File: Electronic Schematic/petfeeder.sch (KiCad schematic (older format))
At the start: 7 parts, among them U2 4022, U6 NE555P

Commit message: Hadware 100%
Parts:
- removed C1: 150uF, symbol Device:C
- removed C2: 10pF, symbol Device:C
- removed R6: 2.2kR, symbol Device:R
- removed R7: 200R, symbol Device:R
- removed U2: 4022, symbol 4xxx:4022
- removed U6: NE555P, Package_DIP:DIP-8_W7.62mm, symbol Timer:NE555P
- removed U?: PIC16F84A-XXP, symbol MCU_Microchip_PIC16:PIC16F84A-XXP
- added C3: 10uF, symbol Device:C
- added C4, C5, C7: C, symbol Device:C
- added C6: CP, symbol Device:CP
- added D1, D2: 1N4001, Diode_THT:D_DO-41_SOD81_P10.16mm_Horizontal, symbol Diode:1N4001
- added J1: Ext. UART Conn., symbol Connector:Conn_01x04_Female
- added J2: Ext. Motor Conn., symbol Connector:Conn_01x02_Male
- added J3: Ext. Servo Conn., symbol Connector:Conn_01x03_Female
- added J5: Ext. Keyboard Conn., symbol Connector:Conn_01x08_Male
- added J6: Ext. Balance Conn., symbol Connector:Conn_01x03_Male
- added J7: Ext. AC Input Conn., symbol Connector:Screw_Terminal_01x02
- added J8: Ext. LCD Conn., symbol Connector:Conn_01x14_Female
- added J9: Flash Setup, symbol Connector_Generic:Conn_02x02_Counter_Clockwise
- added Q1: BC237, Package_TO_SOT_THT:TO-92_Inline, symbol Transistor_BJT:BC237
- added R1, R11, R12, R13, R5: 10kR, symbol Device:R
- added R14: 330R, symbol Device:R
- added R2: R, symbol Device:R
- added R3, R4: 1kR, symbol Device:R
- added RV1: R_POT_TRIM, symbol Device:R_POT_TRIM
- added T1: Transformer_1P_SS, symbol Device:Transformer_1P_SS
- added U1: ESP-12F, RF_Module:ESP-12E, symbol RF_Module:ESP-12F
- added U3: DS1307+, Package_DIP:DIP-8_W7.62mm, symbol Timer_RTC:DS1307+
- added U4: IFX27001TFV33, Package_TO_SOT_SMD:TO-252-3_TabPin2, symbol Regulator_Linear:IFX27001TFV33
- added U5: L7805, symbol Regulator_Linear:L7805
- added U9: 24LC01, symbol Memory_EEPROM:24LC01
- added Y1: 32kHz, symbol Device:Crystal
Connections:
- net +5V: now also J2.2 (Pin_2), J3.1 (Pin_1), J6.1 (Pin_1), R14.1, R3.1, R4.1, RV1.3, U3.3 (VBAT), U3.8 (VCC), U4.3 (I), U9.8 (VCC)
- net GND: now also C3.2, C4.2, C5.2, C6.2, C7.2, J1.4 (Pin_4), J3.3 (Pin_3), J6.3 (Pin_3), J8.1 (Pin_1), J8.5 (Pin_5), Q1.3 (E), R13.2, RV1.1, T1.4 (SC), U1.15 (GND), U3.4 (GND), U4.1 (GND), U5.2 (GND), U9.4 (GND), U9.7 (WP)
- net column1: now also J5.1 (Pin_1)
- net column2: now also J5.2 (Pin_2)
- net column3: now also J5.3 (Pin_3)
- net column4: now also J5.4 (Pin_4)
- new net: R1.1, U1.1 (~RST)
- new net: J9.1 (Pin_1), J9.2 (Pin_2), U1.16 (GPIO15)
- new net: R12.1, U1.17 (GPIO2)
- new net: R11.1, U1.3 (EN)
- new net: U3.1 (X1), Y1.2
- new net: U3.2 (X2), Y1.1
- new net: Q1.2 (B), R2.1
- new net: J1.1 (Pin_1), R5.2
- new net: D1.2 (A), T1.5 (SB)
- new net: J7.2 (Pin_2), T1.1 (AA)
- new net: J7.1 (Pin_1), T1.2 (AB)
- new net: D2.2 (A), T1.3 (SA)
- new net: J8.2 (Pin_2), R14.2
- new net: J9.3 (Pin_3), R13.1
- new net +3.3V_OUT: C7.1, U4.2 (Q)
- new net +3V3: C3.1, R1.2, R11.2, R12.2, U1.8 (VCC)
- new net +5V_OUT: C5.1, U5.3 (OUT)
- new net RET_OUT: C4.1, C6.1, D1.1 (K), D2.1 (K), U5.1 (IN)
- new net RX: J1.3 (Pin_3), U1.21 (GPIO3/RXD)
- new net SCL: R4.2, U1.20 (GPIO5), U3.6 (SCL), U9.6 (SCL)
- new net SDA: R3.2, U1.19 (GPIO4), U3.5 (SDA), U9.5 (SDA)
- new net TX: J1.2 (Pin_2), U1.22 (GPIO1/TXD)
- new net balança: J6.2 (Pin_2), U1.2 (ADC)
- new net clk_lcd: U1.6 (GPIO12)
- new net data4: J8.11 (Pin_11)
- new net data5: J8.12 (Pin_12)
- new net data6: J8.13 (Pin_13)
- new net data7: J8.14 (Pin_14)
- new net en: J8.6 (Pin_6)
- new net flash: R5.1, U1.18 (GPIO0)
- new net line1: J5.5 (Pin_5)
- new net line2: J5.6 (Pin_6)
- new net line3: J5.7 (Pin_7)
- new net line4: J5.8 (Pin_8)
- new net motor: R2.2, U1.4 (GPIO16)
- new net motor-: J2.1 (Pin_1), Q1.1 (C)
- new net rs: J8.4 (Pin_4)
- new net rx_lcd: U1.5 (GPIO14)
- new net servo: J3.2 (Pin_2), J9.4 (Pin_4)
- new net trimpot: J8.3 (Pin_3), RV1.2
- new net tx_lcd: U1.7 (GPIO13)
- no-connect marks 6 -> 14
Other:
- note added: "Engines Circuits"
- note added: "External LCD and Keyboard Circuits"
- note added: "Linear Retifier and Regulator Circuit\n"
- note added: "Main Circuit\n\n"
- note removed: "Keyboard's columns pulser\n"

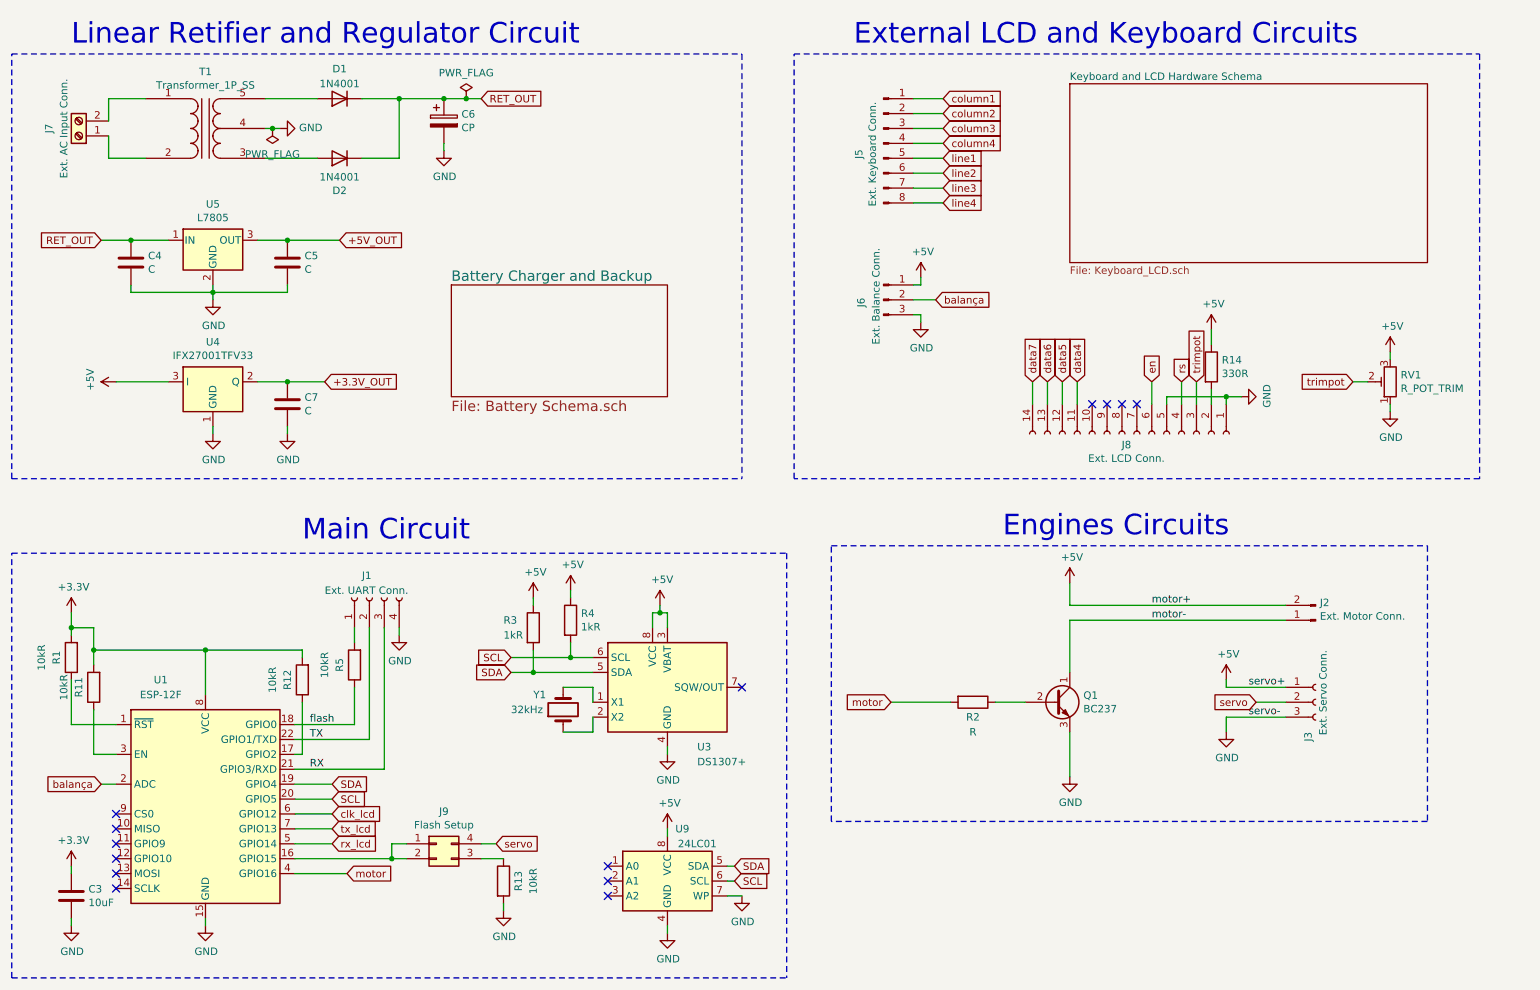
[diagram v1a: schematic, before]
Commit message: Correcoes Esquematico e Avanço codigo esp
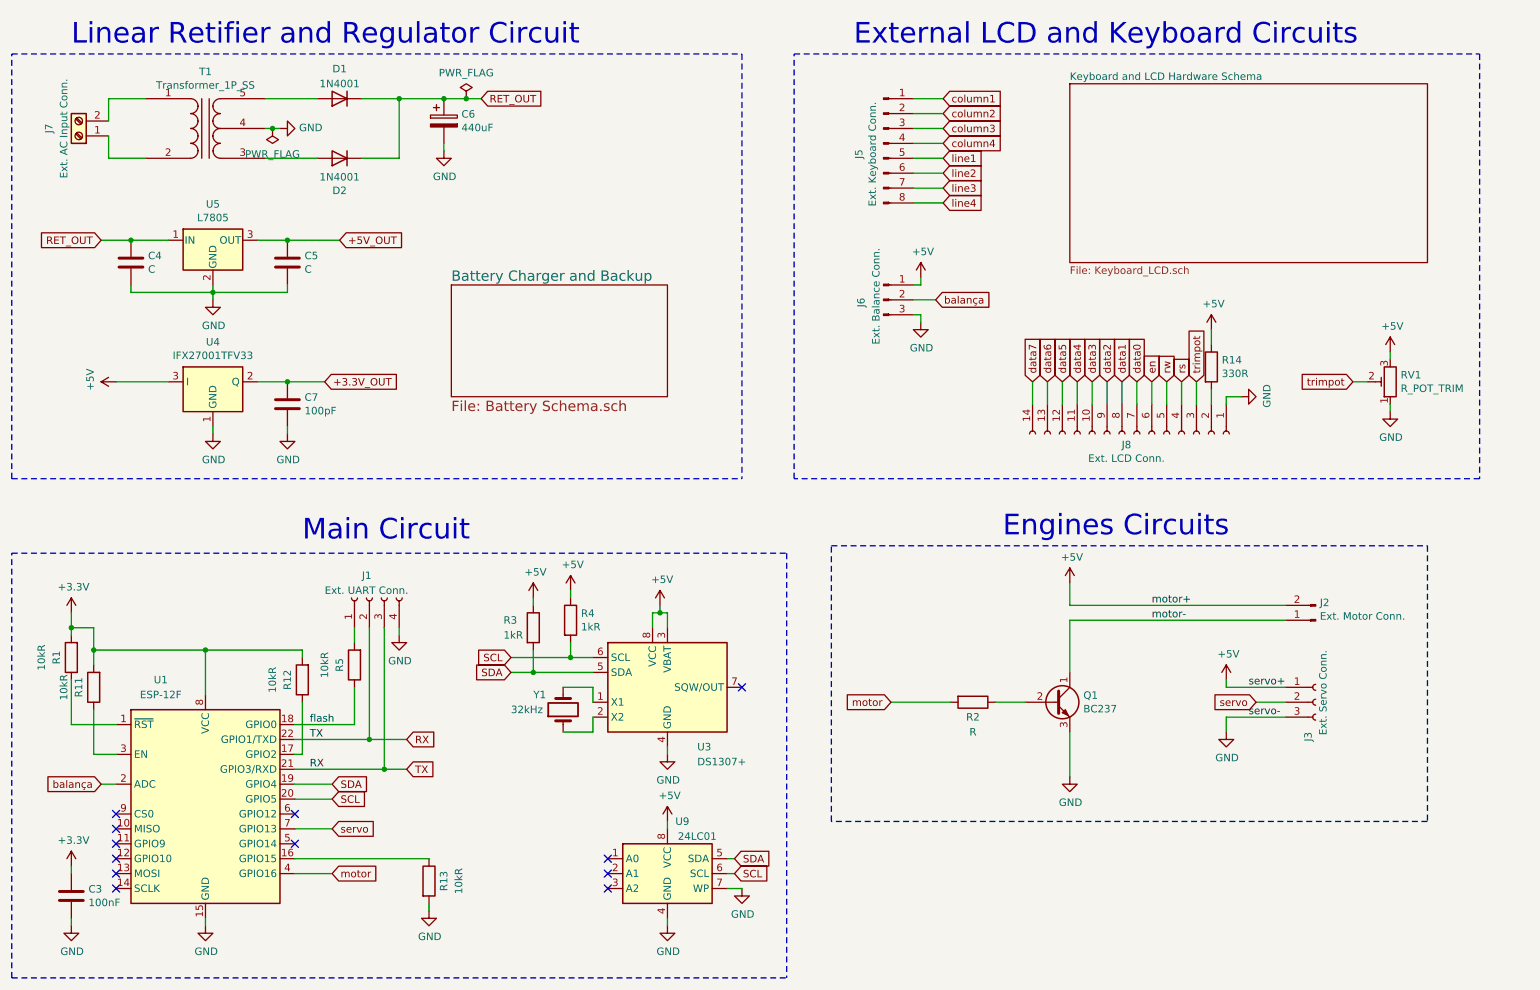
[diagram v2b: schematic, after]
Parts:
- removed J9: Flash Setup, symbol Connector_Generic:Conn_02x02_Counter_Clockwise
- C3: value 10uF -> 100nF
- C6: value CP -> 440uF
- C7: value C -> 100pF
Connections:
- net TX is gone; now on net RX: J1.2 (Pin_2), U1.22 (GPIO1/TXD)
- net tx_lcd is gone; now on net servo: U1.7 (GPIO13)
- net GND: no longer J8.5 (Pin_5)
- net at U1.16 (GPIO15): now also R13.1
- net data3: now reaches J8.10 (Pin_10)
- net data0: now reaches J8.7 (Pin_7)
- net data1: now reaches J8.8 (Pin_8)
- net data2: now reaches J8.9 (Pin_9)
- net clk_lcd: no longer names the net of U1.6 (GPIO12)
- net rx_lcd: no longer names the net of U1.5 (GPIO14)
- new net rw: J8.5 (Pin_5)
- no-connect marks 14 -> 12
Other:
- moved on the sheet: R13, U9
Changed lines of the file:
@@
 Wire Wire Line
 	2300 6900 2300 6850
-Wire Wire Line
-	2900 6550 3250 6550
-Text GLabel 3250 6550 2    50   Input ~ 0
+Text GLabel 3150 6550 2    50   Input ~ 0
 motor
 Text Label 3000 5550 0    50   ~ 0
@@
 Text Notes 6650 1000 0    138  ~ 0
 External LCD and Keyboard Circuits
-Text GLabel 3150 6150 2    50   Input ~ 0
-clk_lcd
-Text GLabel 3150 6250 2    50   Input ~ 0
-tx_lcd
-Text GLabel 3150 6350 2    50   Input ~ 0
-rx_lcd
-Wire Wire Line
-	2900 6350 3150 6350
-Wire Wire Line
-	2900 6250 3150 6250
-Wire Wire Line
-	2900 6150 3150 6150
 Wire Wire Line
 	7050 2050 7250 2050
@@
 P 1400 6700
 F 0 "C3" H 1515 6746 50  0000 L CNN
-F 1 "10uF" H 1515 6655 50  0000 L CNN
+F 1 "100nF" H 1515 6655 50  0000 L CNN
 F 2 "" H 1438 6550 50  0001 C CNN
 F 3 "~" H 1400 6700 50  0001 C CNN
@@
 P 3900 1500
 F 0 "C6" H 4018 1546 50  0000 L CNN
-F 1 "CP" H 4018 1455 50  0000 L CNN
+F 1 "440uF" H 4018 1455 50  0000 L CNN
 F 2 "" H 3938 1350 50  0001 C CNN
 F 3 "~" H 3900 1500 50  0001 C CNN
@@
 P 2850 3400
 F 0 "C7" H 2965 3446 50  0000 L CNN
-F 1 "C" H 2965 3355 50  0000 L CNN
+F 1 "100pF" H 2965 3355 50  0000 L CNN
 F 2 "" H 2888 3250 50  0001 C CNN
 F 3 "~" H 2850 3400 50  0001 C CNN
@@
 EndData
 $EndBitmap
-Text GLabel 4250 6350 2    50   Input ~ 0
+Text GLabel 3150 6250 2    50   Input ~ 0
 servo
 $Comp
-L Connector_Generic:Conn_02x02_Counter_Clockwise J9
-U 1 1 619BBF9D
-P 3850 6350
-F 0 "J9" H 3900 6567 50  0000 C CNN
-F 1 "Flash Setup" H 3900 6476 50  0000 C CNN
-F 2 "" H 3850 6350 50  0001 C CNN
-F 3 "~" H 3850 6350 50  0001 C CNN
-	1    3850 6350
-	1    0    0    -1
-$EndComp
-$Comp
 L Device:R R13
 U 1 1 619DCC8E
-P 4300 6600
-F 0 "R13" V 4400 6600 50  0000 C CNN
-F 1 "10kR" V 4500 6600 50  0000 C CNN
-F 2 "" V 4230 6600 50  0001 C CNN
-F 3 "~" H 4300 6600 50  0001 C CNN
-	1    4300 6600
+P 3800 6600
+F 0 "R13" V 3900 6600 50  0000 C CNN
+F 1 "10kR" V 4000 6600 50  0000 C CNN
+F 2 "" V 3730 6600 50  0001 C CNN
+F 3 "~" H 3800 6600 50  0001 C CNN
+	1    3800 6600
 	1    0    0    -1
 $EndComp
-Wire Wire Line
-	4150 6450 4300 6450
-Wire Wire Line
-	3650 6350 3550 6350
-Wire Wire Line
-	3550 6350 3550 6450
-Connection ~ 3550 6450
-Wire Wire Line
-	3550 6450 3650 6450
 $Comp
 L power:GND #PWR039
 U 1 1 619E8B33
-P 4300 6800
-F 0 "#PWR039" H 4300 6550 50  0001 C CNN
-F 1 "GND" H 4305 6627 50  0000 C CNN
-F 2 "" H 4300 6800 50  0001 C CNN
-F 3 "" H 4300 6800 50  0001 C CNN
-	1    4300 6800
+P 3800 6800
+F 0 "#PWR039" H 3800 6550 50  0001 C CNN
+F 1 "GND" H 3805 6627 50  0000 C CNN
+F 2 "" H 3800 6800 50  0001 C CNN
+F 3 "" H 3800 6800 50  0001 C CNN
+	1    3800 6800
 	1    0    0    -1
 $EndComp
 Wire Wire Line
-	4300 6800 4300 6750
-Wire Wire Line
-	4250 6350 4150 6350
+	3800 6800 3800 6750
 $Comp
 L Device:R R11
@@
 Wire Wire Line
 	8850 3400 8850 3250
-Wire Wire Line
-	9150 3350 8750 3350
-Wire Wire Line
-	8750 3350 8750 3400
-Connection ~ 9150 3350
 Text GLabel 8650 3250 1    50   Input ~ 0
 en
 Wire Wire Line
 	8650 3400 8650 3250
-NoConn ~ 8550 3400
-NoConn ~ 8450 3400
-NoConn ~ 8350 3400
-NoConn ~ 8250 3400
 Text GLabel 8150 3250 1    50   Input ~ 0
 data4
@@
 L Memory_EEPROM:24LC01 U9
 U 1 1 617A6300
-P 5400 6600
-F 0 "U9" H 5500 6950 50  0000 C CNN
-F 1 "24LC01" H 5600 6850 50  0000 C CNN
-F 2 "" H 5400 6600 50  0001 C CNN
-F 3 "http://ww1.microchip.com/downloads/en/DeviceDoc/21711J.pdf" H 5400 6600 50  0001 C CNN
-	1    5400 6600
+P 5400 6550
+F 0 "U9" H 5500 6900 50  0000 C CNN
+F 1 "24LC01" H 5600 6800 50  0000 C CNN
+F 2 "" H 5400 6550 50  0001 C CNN
+F 3 "http://ww1.microchip.com/downloads/en/DeviceDoc/21711J.pdf" H 5400 6550 50  0001 C CNN
+	1    5400 6550
 	1    0    0    -1
 $EndComp
@@
 	4350 5200 4500 5200
 Connection ~ 4500 5200
-Wire Wire Line
-	2900 6450 3550 6450
 $Comp
 L power:GND #PWR048
 U 1 1 617E44D4
-P 5400 6950
-F 0 "#PWR048" H 5400 6700 50  0001 C CNN
-F 1 "GND" H 5405 6777 50  0000 C CNN
-F 2 "" H 5400 6950 50  0001 C CNN
-F 3 "" H 5400 6950 50  0001 C CNN
-	1    5400 6950
+P 5400 6900
+F 0 "#PWR048" H 5400 6650 50  0001 C CNN
+F 1 "GND" H 5405 6727 50  0000 C CNN
+F 2 "" H 5400 6900 50  0001 C CNN
+F 3 "" H 5400 6900 50  0001 C CNN
+	1    5400 6900
 	1    0    0    -1
 $EndComp
@@
 L power:+5V #PWR047
 U 1 1 617EA5A8
-P 5400 6250
-F 0 "#PWR047" H 5400 6100 50  0001 C CNN
-F 1 "+5V" H 5415 6423 50  0000 C CNN
-F 2 "" H 5400 6250 50  0001 C CNN
-F 3 "" H 5400 6250 50  0001 C CNN
-	1    5400 6250
+P 5400 6200
+F 0 "#PWR047" H 5400 6050 50  0001 C CNN
+F 1 "+5V" H 5415 6373 50  0000 C CNN
+F 2 "" H 5400 6200 50  0001 C CNN
+F 3 "" H 5400 6200 50  0001 C CNN
+	1    5400 6200
 	1    0    0    -1
 $EndComp
 Wire Wire Line
-	5400 6300 5400 6250
+	5400 6250 5400 6200
 Wire Wire Line
-	5400 6950 5400 6900
-NoConn ~ 5000 6500
-NoConn ~ 5000 6600
-NoConn ~ 5000 6700
-Text GLabel 5850 6500 2    50   Input ~ 0
+	5400 6900 5400 6850
+NoConn ~ 5000 6450
+NoConn ~ 5000 6550
+NoConn ~ 5000 6650
+Text GLabel 5850 6450 2    50   Input ~ 0
 SDA
-Text GLabel 5850 6600 2    50   Input ~ 0
+Text GLabel 5850 6550 2    50   Input ~ 0
 SCL
 Wire Wire Line
-	5800 6500 5850 6500
+	5800 6450 5850 6450
 Wire Wire Line
-	5800 6600 5850 6600
+	5800 6550 5850 6550
 $Comp
 L Device:Crystal Y1
@@
 $EndComp
 $Comp
-L power:GND #PWR?
+L power:GND #PWR050
 U 1 1 61836966
-P 5900 6700
-F 0 "#PWR?" H 5900 6450 50  0001 C CNN
-F 1 "GND" H 5905 6527 50  0000 C CNN
-F 2 "" H 5900 6700 50  0001 C CNN
-F 3 "" H 5900 6700 50  0001 C CNN
-	1    5900 6700
+P 5900 6650
+F 0 "#PWR050" H 5900 6400 50  0001 C CNN
+F 1 "GND" H 5905 6477 50  0000 C CNN
+F 2 "" H 5900 6650 50  0001 C CNN
+F 3 "" H 5900 6650 50  0001 C CNN
+	1    5900 6650
 	1    0    0    -1
 $EndComp
 Wire Wire Line
-	5800 6700 5900 6700
+	5800 6650 5900 6650
 Wire Notes Line
 	1000 4400 6200 4400
 Wire Notes Line
 	1000 7250 6200 7250
+Text GLabel 3650 5650 2    50   Input ~ 0
+RX
+Text GLabel 3650 5850 2    50   Input ~ 0
+TX
+Wire Wire Line
+	3650 5850 3500 5850
+Connection ~ 3500 5850
+Wire Wire Line
+	3650 5650 3400 5650
+Connection ~ 3400 5650
+NoConn ~ 2900 6150
+NoConn ~ 2900 6350
+Text GLabel 8550 3250 1    50   Input ~ 0
+data0
+Text GLabel 8450 3250 1    50   Input ~ 0
+data1
+Text GLabel 8350 3250 1    50   Input ~ 0
+data2
+Text GLabel 8250 3250 1    50   Input ~ 0
+data3
+Wire Wire Line
+	8250 3400 8250 3250
+Wire Wire Line
+	8350 3400 8350 3250
+Wire Wire Line
+	8450 3400 8450 3250
+Wire Wire Line
+	8550 3400 8550 3250
+Wire Wire Line
+	2900 6250 3150 6250
+Wire Wire Line
+	2900 6450 3800 6450
+Text GLabel 8750 3250 1    50   Input ~ 0
+rw
+Wire Wire Line
+	8750 3250 8750 3400
+Wire Wire Line
+	3150 6550 2900 6550
 $EndSCHEMATC
